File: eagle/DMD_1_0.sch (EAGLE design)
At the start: 26 parts, among them X1 Col, X2 Row

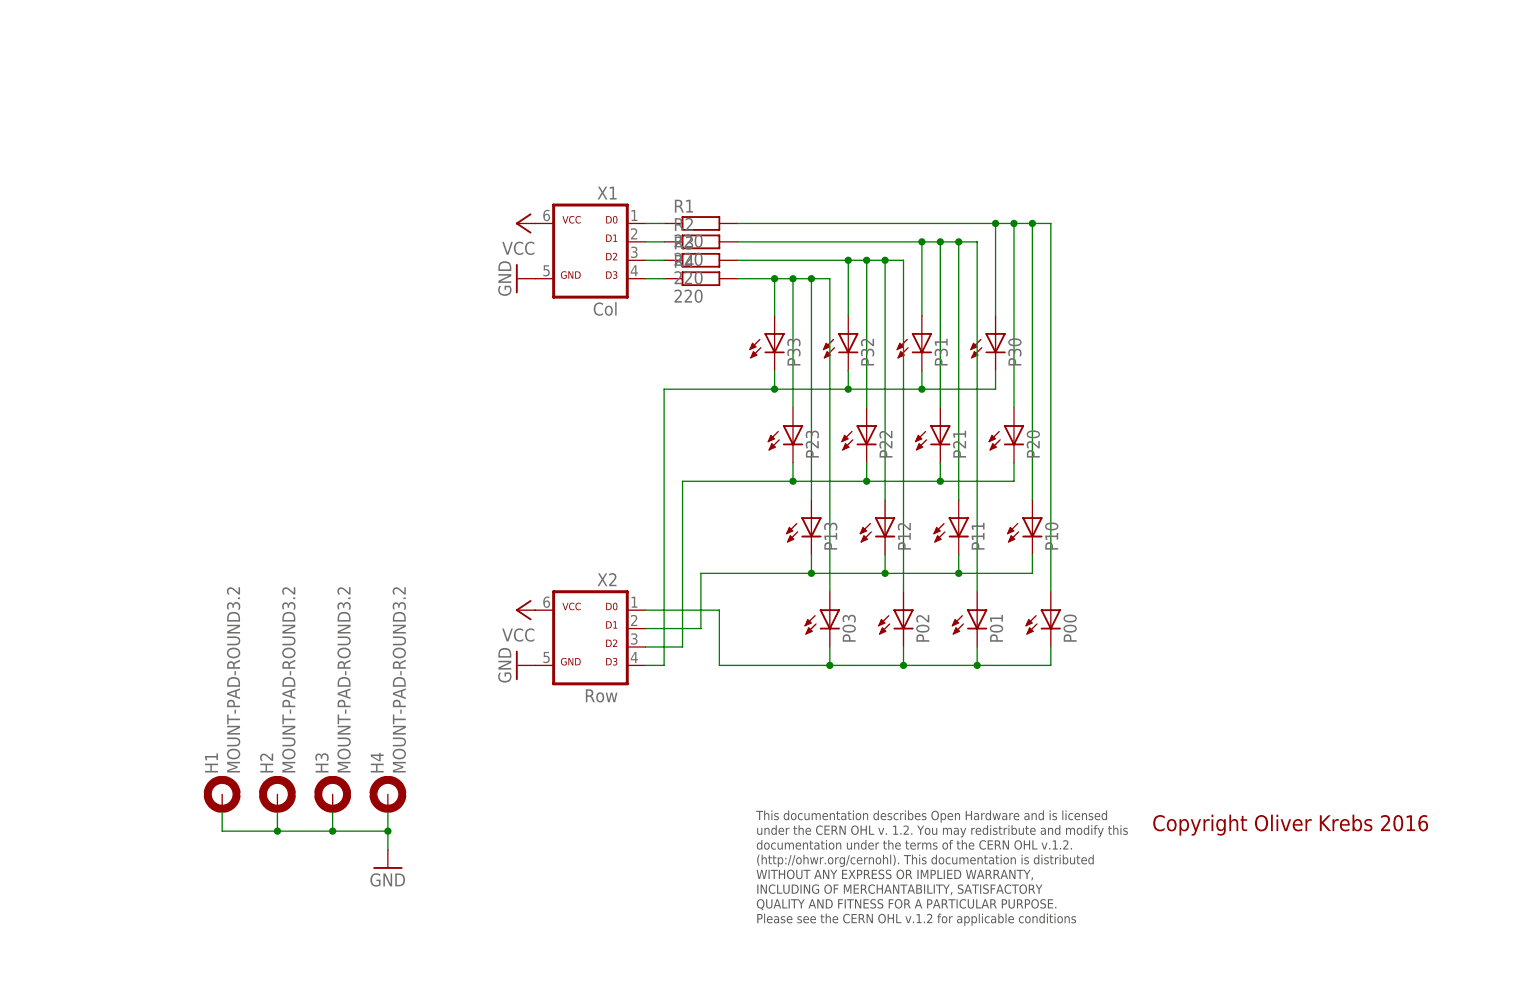
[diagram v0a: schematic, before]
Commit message: Add new tetra-Board and arduino files
Add AMP_1_0, AVC_1_0, D18_1_1, IOP_1_2, MIC_1_0, PIN_1_1, POT_1_0, PWA_1_0, PWR_1_0, RGF 2.0, SOC_2_0, VLT_1_0
Add mex_nano_shield_keyboard, mex_nano_shied_numbers

New arduino projects
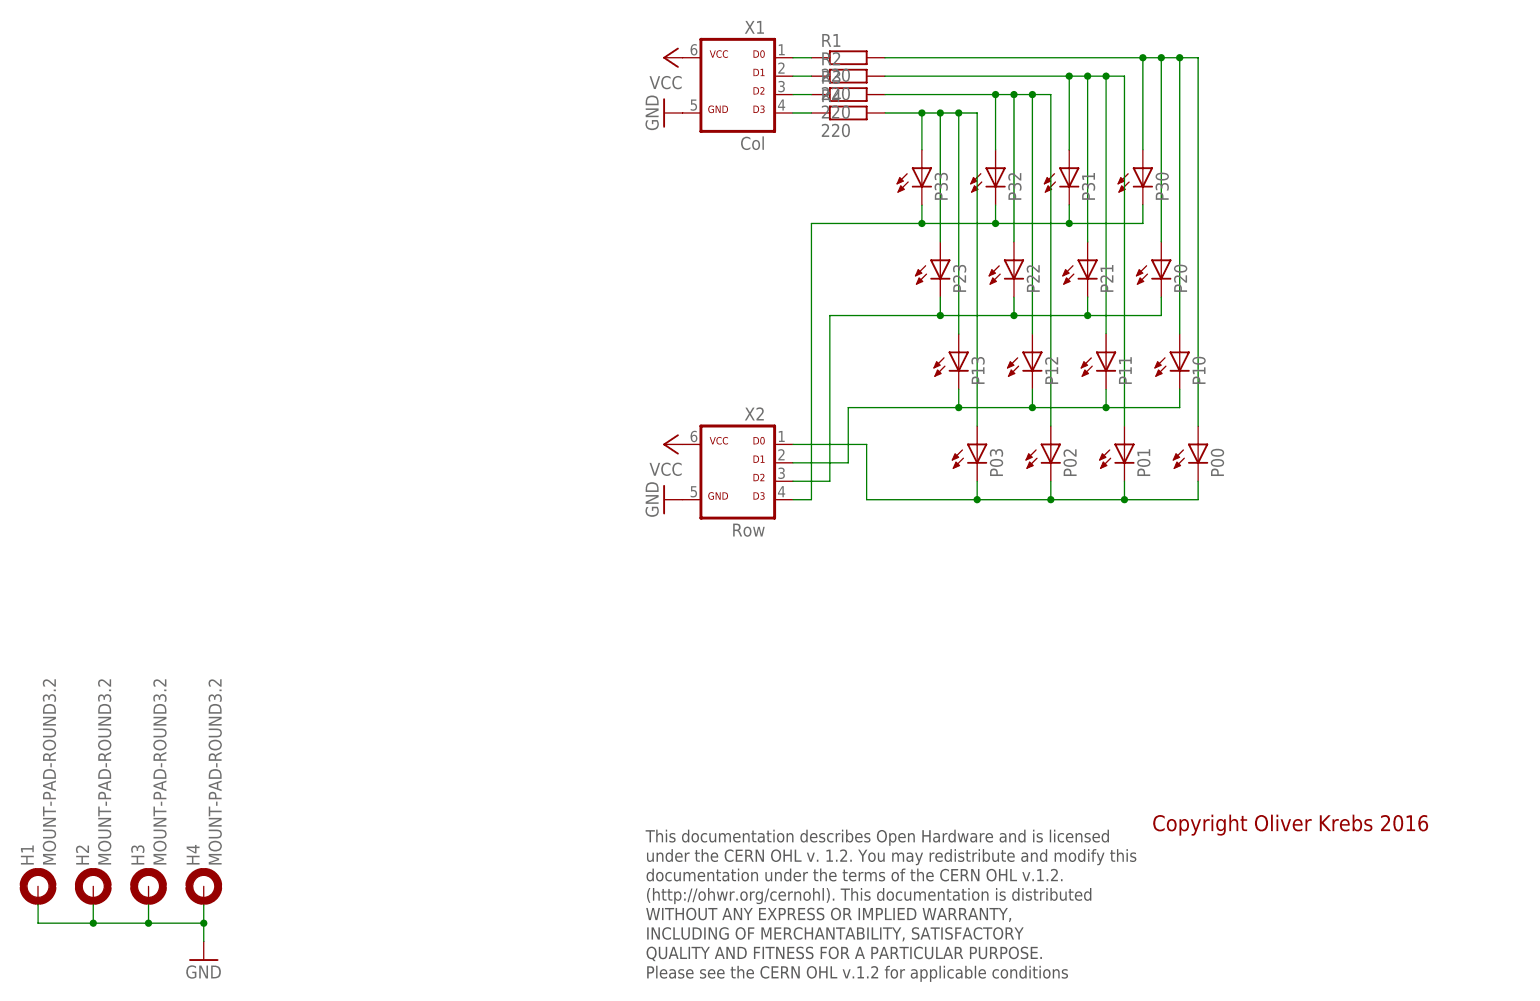
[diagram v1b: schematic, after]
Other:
- moved on the sheet: H1, H2, H3, H4, P00, P01, P02, P03, P10, P11, P12, P13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
